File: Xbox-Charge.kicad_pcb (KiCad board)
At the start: 13 copper layers, 38.5 x 38.5 mm, 90 parts, among them J1 Conn_01x04_Pin, J2 Conn_01x04_Pin, Q1 CSD17551Q3A, Q2 CSD17551Q3A, Q3 CSD17551Q3A, Q4 CSD17551Q3A, Q5 CSD25402Q3A, U1 TPS25750D, U2 BQ25713RSNR, U3 CAT24C512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

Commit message: Initial commit
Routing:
- net GND: track 31.7 -> 30.8 mm
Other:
- outline, holes or cut-outs redrawn
- copper layers 13 -> 4
- board text added: "OUT+"

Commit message: misc
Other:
- board text added: "SDA SCL"
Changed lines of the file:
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@@
 		)
 	)
+	(gr_text "SDA\nSCL"
+		(at 156.5 55.75 90)
+		(layer "F.SilkS")
+		(effects
+			(font
+				(size 0.75 0.75)
+				(thickness 0.09375)
+			)
+			(justify right)
+		)
+	)
 	(gr_text "VBUS"
 		(at 156.24 33.73 0)
@@
 	)
 	(segment
-		(start 175.56 45.7)
-		(end 175.56 43.86)
-		(width 0.2)
-		(layer "B.Cu")
-		(net 5)
-	)
-	(segment
 		(start 172.03 49.5)
-		(end 172.03 49.23)
+		(end 175.56 45.97)
 		(width 0.2)
 		(layer "B.Cu")
@@
 	)
 	(segment
-		(start 172.03 49.23)
-		(end 175.56 45.7)
+		(start 175.56 45.97)
+		(end 175.56 43.86)
 		(width 0.2)
 		(layer "B.Cu")
@@
 	)
 	(segment
-		(start 153.65 40.53)
-		(end 152.93 41.25)
-		(width 0.5)
-		(layer "In1.Cu")
-		(net 16)
-	)
-	(segment
-		(start 161.07 50.11)
-		(end 161.07 51.19)
+		(start 161.07 51.18)
+		(end 158.64 53.61)
 		(width 0.5)
 		(layer "In1.Cu")
@@
 	)
 	(segment
-		(start 162.095 49.085)
-		(end 161.07 50.11)
+		(start 153.65 40.53)
+		(end 152.93 41.25)
 		(width 0.5)
 		(layer "In1.Cu")
@@
 	)
 	(segment
-		(start 158.63 53.61)
-		(end 157.95 53.61)
+		(start 162.095 49.085)
+		(end 161.07 50.11)
 		(width 0.5)
 		(layer "In1.Cu")
@@
 	)
 	(segment
-		(start 152.93 43.97)
-		(end 154.45 45.49)
+		(start 161.07 50.11)
+		(end 161.07 51.18)
 		(width 0.5)
 		(layer "In1.Cu")
@@
 	)
 	(segment
-		(start 158.64 53.62)
-		(end 158.63 53.61)
+		(start 152.93 43.97)
+		(end 154.45 45.49)
 		(width 0.5)
 		(layer "In1.Cu")
@@
 	)
 	(segment
-		(start 154.74 53.61)
-		(end 154.72 53.63)
+		(start 158.64 53.61)
+		(end 157.95 53.61)
 		(width 0.5)
 		(layer "In1.Cu")
@@
 	)
 	(segment
-		(start 162.47 45.96)
-		(end 162.095 46.335)
+		(start 154.74 53.61)
+		(end 154.72 53.63)
 		(width 0.5)
 		(layer "In1.Cu")
@@
 	)
 	(segment
-		(start 161.07 51.19)
-		(end 158.64 53.62)
+		(start 162.47 45.96)
+		(end 162.095 46.335)
 		(width 0.5)
 		(layer "In1.Cu")
@@
 	)
 	(segment
+		(start 158.79 46.76)
+		(end 160.87 46.76)
+		(width 0.5)
+		(layer "F.Cu")
+		(net 23)
+	)
+	(segment
 		(start 160.875 46.755)
 		(end 160.875 52.077462)
@@
 		(width 0.5)
 		(layer "F.Cu")
-		(net 23)
-	)
-	(segment
-		(start 158.79 46.76)
-		(end 160.87 46.76)
-		(width 0.5)
-		(layer "F.Cu")

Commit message: Slight changes, may need to largely redesign
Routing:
- net GND: track 30.8 -> 29.8 mm
- net /VSYS: vias 86 -> 140
- added copper zone on In1.Cu, net /VSYS
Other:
- board text added: "VOUT"
- board text removed: "OUT+"

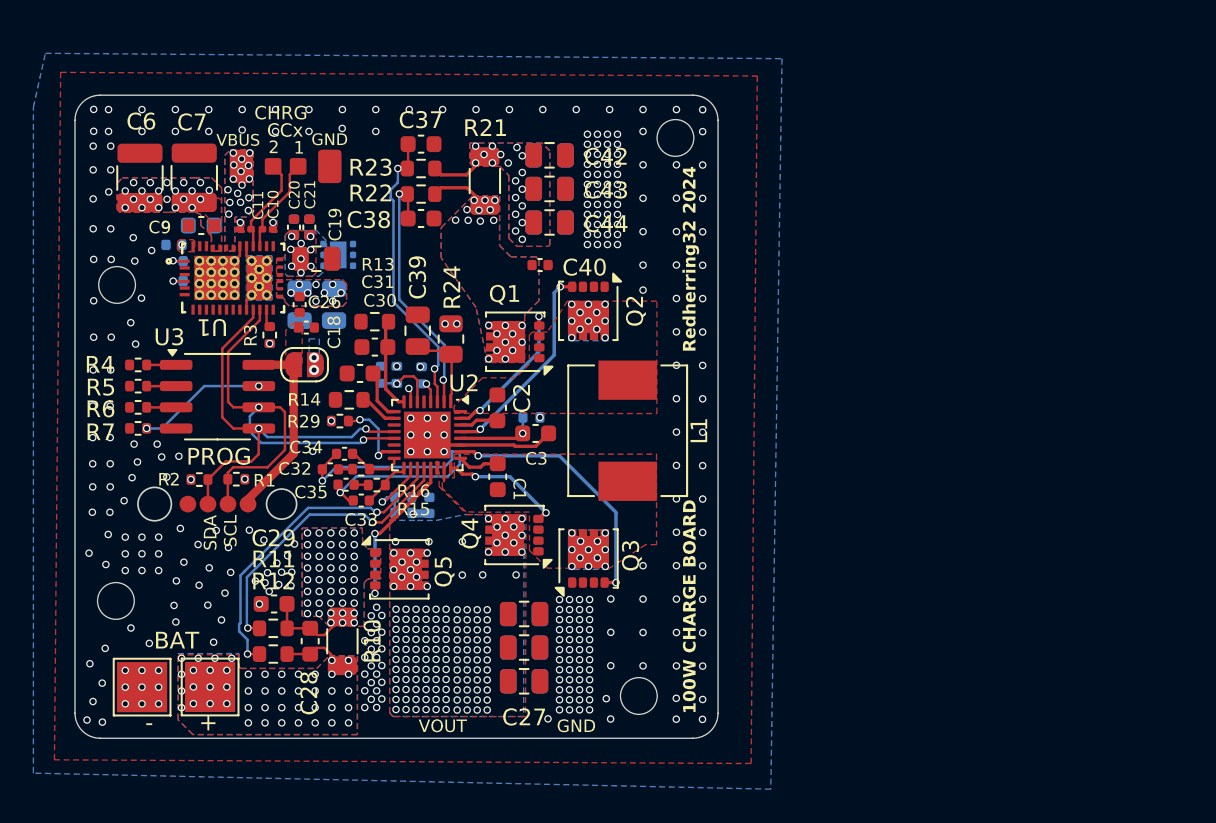
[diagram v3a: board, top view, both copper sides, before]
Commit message: Remove USB-C controller, planning to use MelonHD
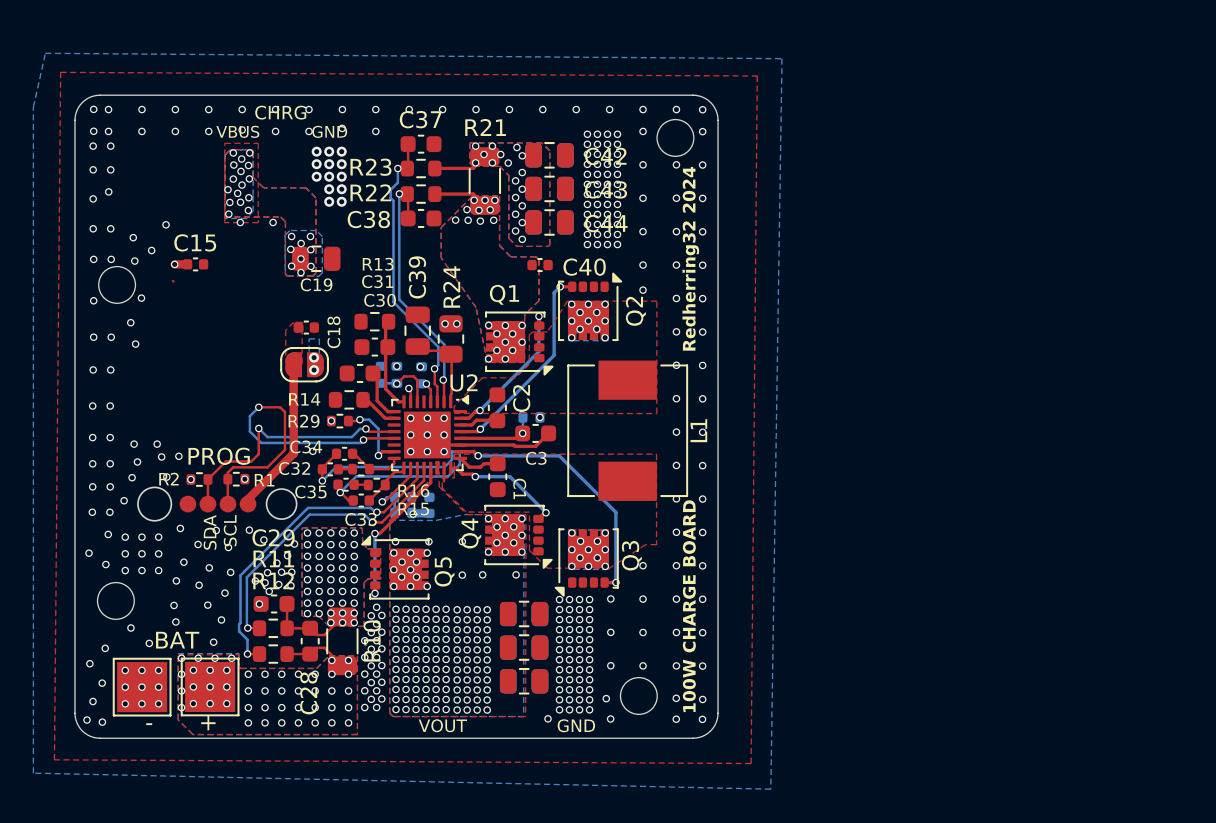
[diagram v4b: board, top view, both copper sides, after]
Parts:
- removed C10, C11: 330pF, Capacitor_SMD:C_0201_0603Metric
- removed C16, C17: 10uF, Capacitor_SMD:C_0402_1005Metric
- removed C20, C21, C22, C23: 0.01uF, Capacitor_SMD:C_0402_1005Metric
- removed C24, C25: 22uF, Capacitor_SMD:C_0805_2012Metric
- removed C26: 0.1uF, Capacitor_SMD:C_0402_1005Metric
- removed C6, C7: 100uF, Capacitor_SMD:C_1210_3225Metric
- removed C8, C9: 10uF, Capacitor_SMD:C_0603_1608Metric
- removed J2: Conn_01x04_Pin, Xbox-Charge:VBUS PADS
- removed R3, R4, R5, R6, R7: 10K, Resistor_SMD:R_0402_1005Metric
- removed U1: TPS25750D, Xbox-Charge:TPS25750D
- removed U3: CAT24C512, Package_SO:SOIC-8_3.9x4.9mm_P1.27mm
- removed U4: TVS2200DRV, Package_SON:WSON-6-1EP_2x2mm_P0.65mm_EP1x1.6mm
- C15: moved to F.Cu
- R18: value 383K -> 100K
- R19: value 220K -> 150K
- R8: value 750K -> 300K
- R9: value 250K -> 100K
- moved C15 0.32 mm to (155.0, 40.8)
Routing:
- net /SDA: track 24.9 -> 15.3 mm
- net /SCL: track 28.8 -> 20.5 mm
- net Net-(U3-WP): track 7.77 -> 0.00 mm, vias 2 -> 0
- net /CC2: track 5.80 -> 0.00 mm
- net /CC1: track 5.73 -> 0.00 mm
- net /EEPROM_3V3: track 11.6 -> 9.48 mm
- net /DRAIN: track 2.02 -> 0.00 mm
- net Net-(U3-A2): track 1.77 -> 0.00 mm
- net Net-(U3-A1): track 1.77 -> 0.00 mm
- net Net-(U3-A0): track 1.77 -> 0.00 mm
- net /LDO_3V3: track 36.2 -> 34.8 mm, vias 8 -> 7
- net /LDO_1V5: track 1.30 -> 0.00 mm, vias 1 -> 0
- net /~{IRQ}: track 1.04 -> 0.00 mm
- net GND: track 29.8 -> 28.8 mm, vias 315 -> 328
- net /PPHV: vias 9 -> 0
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- removed copper zone on F.Cu, net /3V3
- removed copper zone on B.Cu, net /DRAIN
- removed copper zone on B.Cu, net /PP5V
- removed copper zone on F.Cu, net /PP5V
- removed copper zone on B.Cu, net /PPHV
- removed copper zone on F.Cu, net /PPHV
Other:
- board text removed: "1"
- board text removed: "2"
- board text removed: "CCx"

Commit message: Trim corner
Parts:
- moved REF** 32.9 mm to (150.8, 33.3), turned to 90 degrees
- moved TP3 31.9 mm to (183.7, 65.2), turned to 90 degrees
- moved REF** 31.2 mm to (184.2, 35.5), turned to 90 degrees
- moved REF** 28.9 mm to (178.5, 66.8), turned to 90 degrees
- moved TP2 28.2 mm to (183.7, 61.2), turned to 90 degrees
- moved REF** 26.4 mm to (159.6, 66.7), turned to 90 degrees
- moved C42 25.2 mm to (151.8, 40.8), turned to 90 degrees
- moved C47 25.2 mm to (151.8, 40.8), turned to 90 degrees
- moved C12 24.9 mm to (183.3, 42.4), turned to 90 degrees
- moved C27 24.9 mm to (183.3, 42.4), turned to 90 degrees
- moved R12 23.1 mm to (181.7, 57.4), turned to -90 degrees
- moved C37 22.9 mm to (151.2, 48.5), turned to 90 degrees
- moved C43 22.8 mm to (153.9, 40.8), turned to 90 degrees
- moved C46 22.8 mm to (153.9, 40.8), turned to 90 degrees
- moved C13 22.4 mm to (181.3, 42.4), turned to 90 degrees
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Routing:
- net GND: vias 328 -> 311
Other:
- outline, holes or cut-outs redrawn

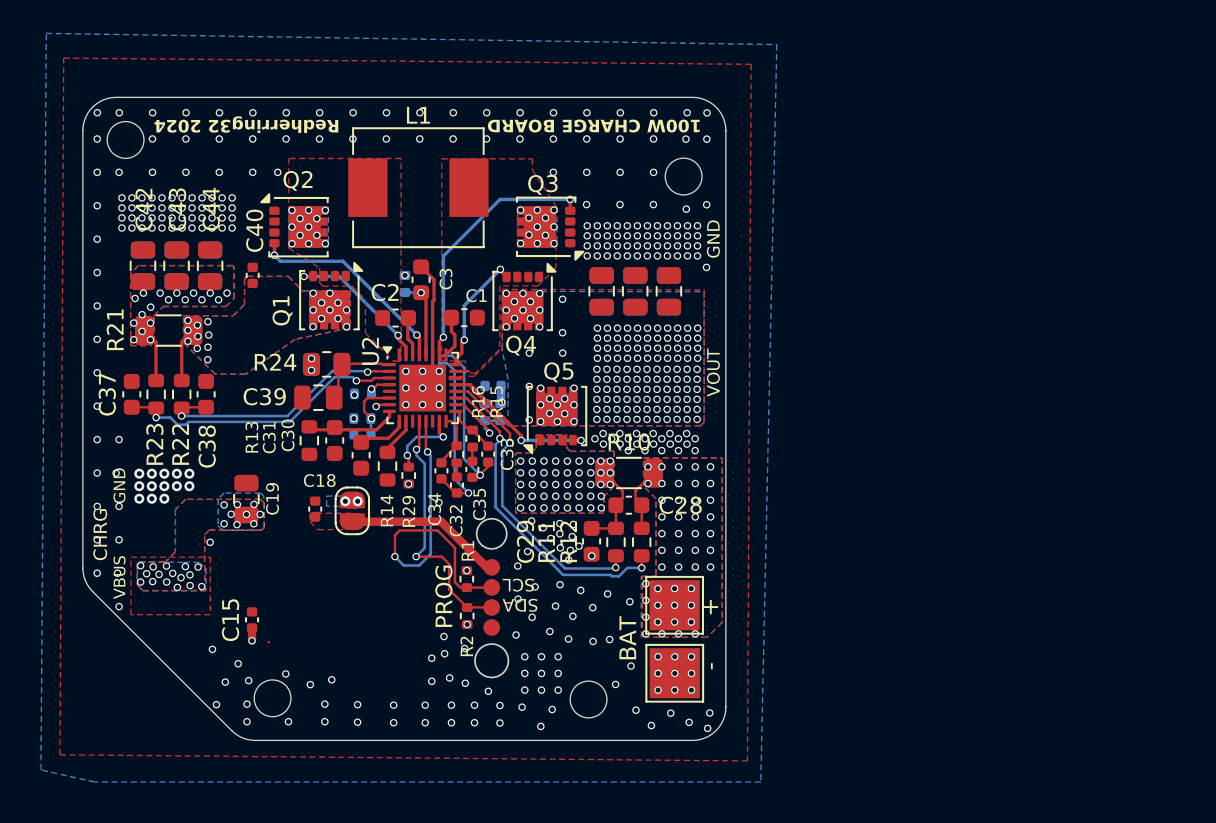
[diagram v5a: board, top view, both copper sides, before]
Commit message: Rework 100W charge PCB, begin adding protection
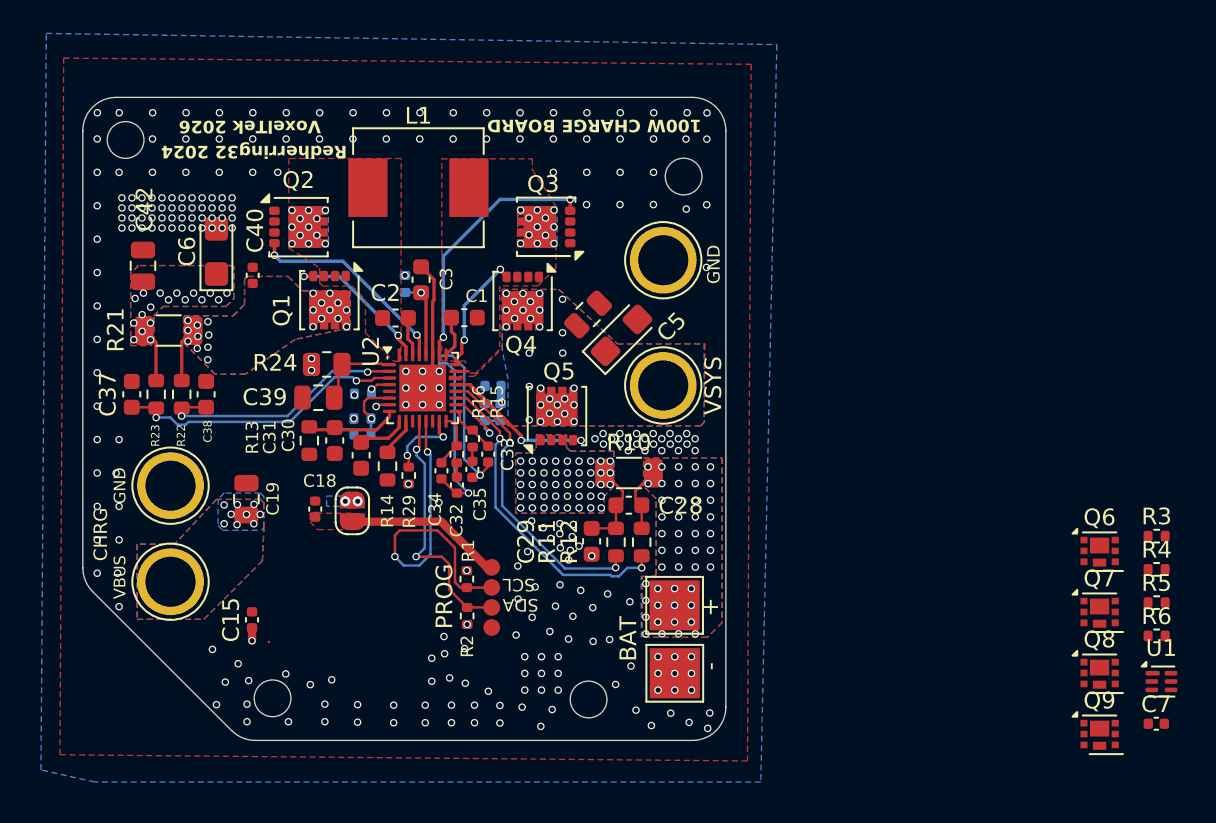
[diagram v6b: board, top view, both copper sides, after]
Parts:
- removed C12, C13, C14, C27, C43, C44, C45, C46, C47: 10uF, Capacitor_SMD:C_0805_2012Metric
- added C6: 100uF, Capacitor_Tantalum_SMD:CP_EIA-3216-18_Kemet-A, F.Cu at (156.2, 40.0)
- added C7: 0.1uF, Capacitor_SMD:C_0402_1005Metric, F.Cu at (212.5, 68.2)
- added Q6: DMT3006, Package_DFN_QFN:Diodes_UDFN2020-6_Type-F, F.Cu at (209.1, 57.9)
- added Q7: DMT3006, Package_DFN_QFN:Diodes_UDFN2020-6_Type-F, F.Cu at (209.1, 61.6)
- added Q8: DMT3006, Package_DFN_QFN:Diodes_UDFN2020-6_Type-F, F.Cu at (209.1, 65.2)
- added Q9: DMT3006, Package_DFN_QFN:Diodes_UDFN2020-6_Type-F, F.Cu at (209.1, 68.9)
- added R3: 330, Resistor_SMD:R_0402_1005Metric, F.Cu at (212.5, 57.0)
- added R4: 2.2k, Resistor_SMD:R_0402_1005Metric, F.Cu at (212.5, 59.0)
- added R5: 100k, Resistor_SMD:R_0402_1005Metric, F.Cu at (212.5, 61.0)
- added R6: 100k, Resistor_SMD:R_0402_1005Metric, F.Cu at (212.5, 63.0)
- added TP4: VBUS, TestPoint:TestPoint_Plated_Hole_D3.0mm, F.Cu at (153.5, 59.8)
- added TP5: GND, TestPoint:TestPoint_Plated_Hole_D3.0mm, F.Cu at (153.5, 54.0)
- added TP6: VSYS, TestPoint:TestPoint_Plated_Hole_D3.0mm, F.Cu at (183.0, 48.0)
- added TP7: GND, TestPoint:TestPoint_Plated_Hole_D3.0mm, F.Cu at (183.0, 40.5)
- added U1: BQ297xy, Package_SON:WSON-6_1.5x1.5mm_P0.5mm, F.Cu at (212.8, 65.7)
- C5: value 10uF -> 100uF; footprint Capacitor_SMD:C_0805_2012Metric -> Capacitor_Tantalum_SMD:CP_EIA-3216-18_Kemet-A
- moved C4 3.14 mm to (178.5, 43.8), turned to 45 degrees
- moved C5 2.90 mm to (180.5, 45.0), turned to 45 degrees
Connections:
- net /VBUS renamed VBUS
- net /VSYS renamed VCC
- net Net-(BT1-+) renamed /BATT+
- TP3 pad 1: GND -> /BATT-
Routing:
- net VCC: vias 140 -> 30
- net VBUS: vias 45 -> 29
- net GND: vias 311 -> 240
- net /BATT-: vias 0 -> 9
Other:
- board text added: "VoxelTek 2026"
- board text removed: "VOUT"

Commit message: misc improvements
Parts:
- removed Q9: DMT3006, Package_DFN_QFN:Diodes_UDFN2020-6_Type-F
- removed R6: 100k, Resistor_SMD:R_0402_1005Metric
- removed the REF** at (178.5, 66.8)
- added C8: 100uF, Capacitor_Tantalum_SMD:CP_EIA-3216-18_Kemet-A, F.Cu at (179.0, 43.8)
- added C9: 100uF, Capacitor_Tantalum_SMD:CP_EIA-3216-18_Kemet-A, F.Cu at (154.0, 40.5)
- added D1: BAT54C, Package_TO_SOT_SMD:SOT-23-3, F.Cu at (166.5, 64.8)
- added R7: 100k, Resistor_SMD:R_0402_1005Metric, F.Cu at (163.2, 64.8)
- added TP8: ~{SHIP}, TestPoint:TestPoint_Pad_D1.5mm, F.Cu at (171.0, 68.0)
- moved R5 48.8 mm to (163.8, 62.2), turned to 90 degrees
- moved U1 34.5 mm to (178.5, 62.2)
- moved Q8 33.9 mm to (175.2, 65.2), turned to 90 degrees
- moved R4 33.8 mm to (178.8, 60.8)
- moved C7 32.0 mm to (181.0, 62.5), turned to -90 degrees
- moved R3 31.7 mm to (181.0, 60.5), turned to 90 degrees
- moved Q7 31.6 mm to (177.8, 65.2), turned to -90 degrees
- moved Q6 29.8 mm to (180.2, 65.2), turned to 90 degrees
- moved C4 6.54 mm to (179.6, 50.2), turned to -90 degrees
- moved C6 0.52 mm to (156.2, 40.5)
- moved C5 0.25 mm to (180.5, 45.2)
- moved TP6 0.20 mm to (183.2, 48.0)
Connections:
- Q8 pad 3: Net-(Q8-G) -> ~{SHIP}
- R5 pad 1: Net-(Q8-G) -> Net-(D1-Pad1)
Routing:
- net VCC: track 0.00 -> 28.8 mm
- net ~{SHIP}: track 0.00 -> 11.5 mm
- net Net-(Q6-G): track 0.00 -> 8.78 mm, vias 0 -> 2
- net VBUS: track 3.29 -> 11.1 mm, vias 29 -> 39
- net /BATT-_2: track 0.00 -> 4.82 mm, vias 0 -> 2
- net Net-(U1-BAT): track 0.00 -> 3.45 mm
- net /BATT-: track 0.00 -> 3.35 mm, vias 9 -> 11
- net Net-(Q7-G): track 0.00 -> 2.64 mm
- net Net-(D1-Pad1): track 0.00 -> 2.04 mm
- net Net-(D1-Pad2): track 0.00 -> 2.00 mm
- net Net-(U1-V-): track 0.00 -> 1.08 mm
- net /BATT+: track 3.91 -> 4.92 mm
- net Net-(Q6-D-Pad1): vias 0 -> 6
- net GND: vias 240 -> 228
- added copper zone on B.Cu, net /BATT-
- added copper zone on F.Cu, net /BATT-
- added copper zone on In1.Cu, net /BATT-
- added copper zone on B.Cu, net /BATT-_2
- added copper zone on F.Cu, net /BATT-_2
- added copper zone on In1.Cu, net /BATT-_2
- added copper zone on B.Cu, net Net-(Q6-D-Pad1)
- added copper zone on F.Cu, net Net-(Q6-D-Pad1)
- added copper zone on In1.Cu, net Net-(Q6-D-Pad1)
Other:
- board text removed: "BAT"
